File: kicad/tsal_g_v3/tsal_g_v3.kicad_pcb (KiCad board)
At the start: 2 copper layers, 55 x 50 mm, 54 parts, among them J1 Conn_01x02_Pin, J2 Conn_01x02_Pin, J3 Conn_01x03, J4 Conn_01x06, Q1 2N7002, Q2 2N7002, Q4 AO3401A, U1 LTV-817S, U10 TL431DBZ, U3 B1212, U4 BU4SU69G2, U5 BUS4S71G2, U6 BU4S81G2, U7 BU4S81G2, U8 BU4S01G2, U9 BU4S01G2

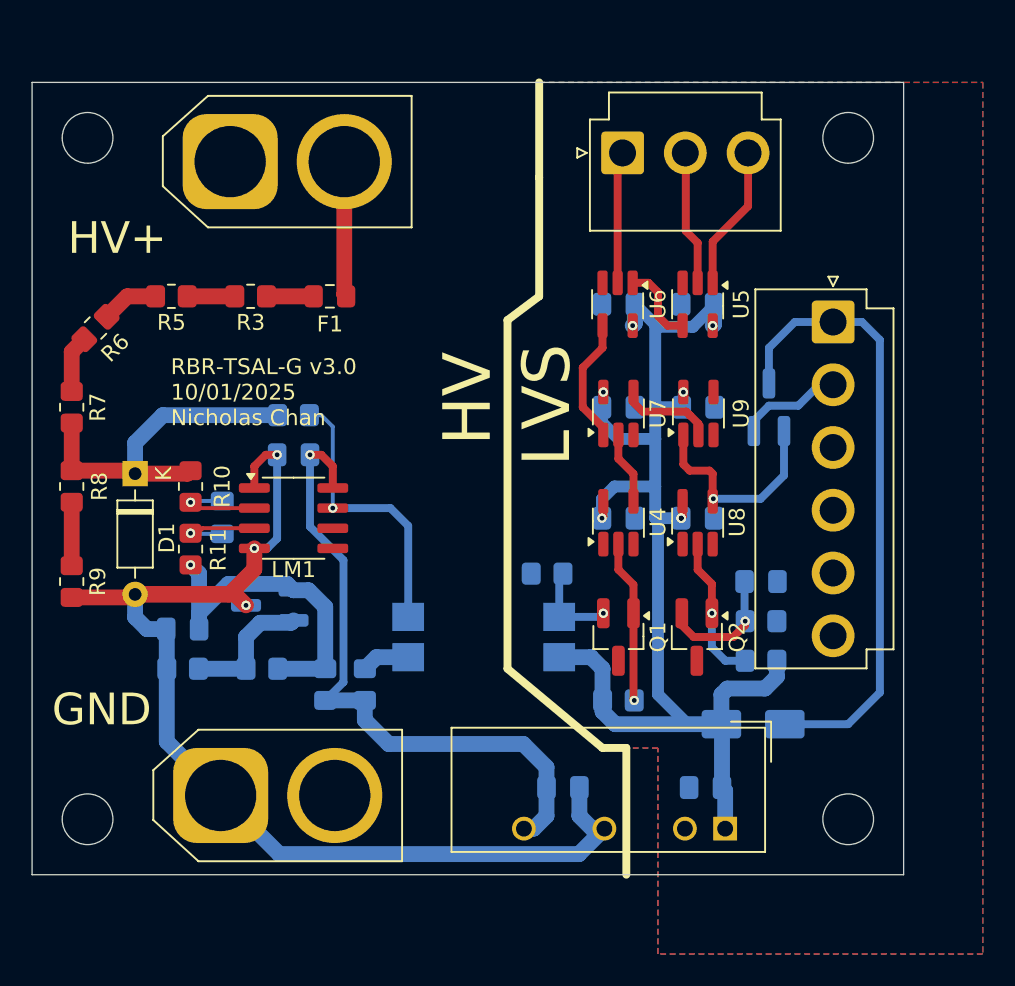
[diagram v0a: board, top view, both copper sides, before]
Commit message: hole seperation to multiples of 3mm
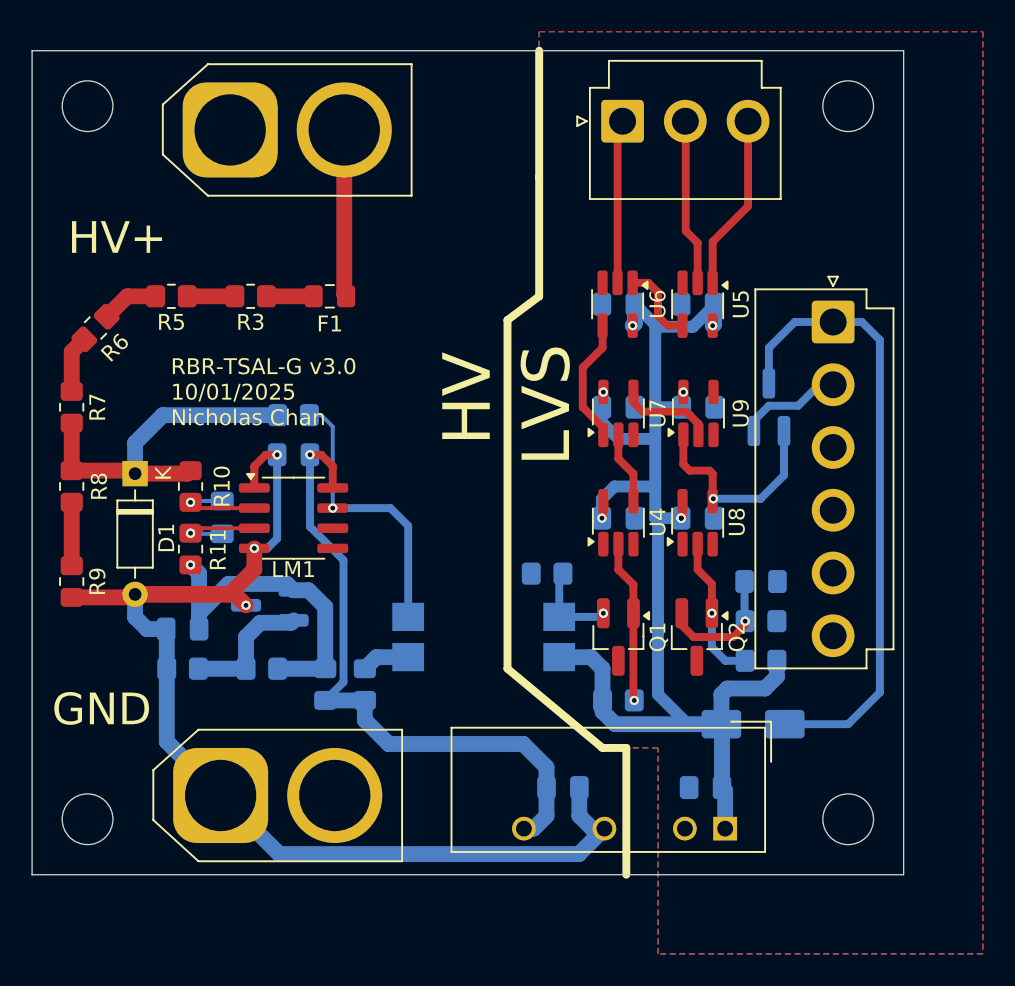
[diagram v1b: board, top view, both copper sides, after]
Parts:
- moved H1 2.00 mm to (153.5, 51.5)
- moved H2 2.00 mm to (201.5, 51.5)
- moved J1 2.00 mm to (162.5, 53.0)
- moved J3 2.00 mm to (187.3, 52.5)
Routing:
- net Out Precharge: track 8.52 -> 10.5 mm
- net Out -: track 8.33 -> 10.3 mm
- net Out +: track 9.12 -> 11.1 mm
- net Net-(J1-Pin_2): track 8.55 -> 10.5 mm
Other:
- board size 55 x 50 mm -> 55 x 52 mm
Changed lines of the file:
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@@
 	(footprint "Connector_JST:JST_VH_B3P-VH_1x03_P3.96mm_Vertical"
 		(layer "F.Cu")
-		(at 187.2625 54.45)
+		(at 187.2625 52.45)
 		(descr "JST VH series connector, B3P-VH (http://www.jst-mfg.com/product/pdf/eng/eVH.pdf), generated with kicad-footprint-generator")
 		(tags "connector JST VH vertical")
@@
 	(footprint "MountingHole:MountingHole_3.2mm_M3"
 		(layer "F.Cu")
-		(at 201.5 53.5)
+		(at 201.5 51.5)
 		(descr "Mounting Hole 3.2mm, no annular, M3")
 		(tags "mounting hole 3.2mm no annular m3")
@@
 	(footprint "Connector_AMASS:AMASS_XT60-M_1x02_P7.20mm_Vertical"
 		(layer "F.Cu")
-		(at 162.5 55)
+		(at 162.5 53)
 		(descr "AMASS female XT60, through hole, vertical, https://www.tme.eu/Document/2d152ced3b7a446066e6c419d84bb460/XT60%20SPEC.pdf")
 		(tags "XT60 female vertical")
@@
 		(tags "SOT-23-5 hand-soldering")
 		(property "Reference" "U8"
-			(at 0.036666 2.5 270)
+			(at 0.036666 2.5 -90)
 			(layer "F.SilkS")
 			(effects
@@
 		)
 		(property "Value" "BU4S01G2"
-			(at 0 2.9 270)
+			(at 0 2.9 -90)
 			(layer "F.Fab")
 			(effects
@@
 		)
 		(fp_text user "${REFERENCE}"
-			(at 0 0 360)
+			(at 0 0 0)
 			(layer "F.Fab")
 			(effects
@@
 		(tags "resistor handsolder")
 		(property "Reference" "R10"
-			(at 0 2 270)
+			(at 0 2 -90)
 			(layer "F.SilkS")
 			(effects
@@
 		)
 		(property "Value" "100"
-			(at 0 1.65 270)
+			(at 0 1.65 -90)
 			(layer "F.Fab")
 			(effects
@@
 		)
 		(fp_text user "${REFERENCE}"
-			(at 0 0 270)
+			(at 0 0 -90)
 			(layer "F.Fab")
 			(effects
@@
 		(tags "SOT-23-5 hand-soldering")
 		(property "Reference" "U7"
-			(at 0 2.5 270)
+			(at 0 2.5 -90)
 			(layer "F.SilkS")
 			(effects
@@
 		)
 		(property "Value" "BU4S81G2 "
-			(at 0 2.9 270)
+			(at 0 2.9 -90)
 			(layer "F.Fab")
 			(effects
@@
 		)
 		(fp_text user "${REFERENCE}"
-			(at 0 0 360)
+			(at 0 0 0)
 			(layer "F.Fab")
 			(effects
@@
 		(tags "resistor handsolder")
 		(property "Reference" "R8"
-			(at 0 1.75 270)
+			(at 0 1.75 -90)
 			(layer "F.SilkS")
 			(effects
@@
 		)
 		(property "Value" "25k"
-			(at 0 1.65 270)
+			(at 0 1.65 -90)
 			(layer "F.Fab")
 			(effects
@@
 		)
 		(fp_text user "${REFERENCE}"
-			(at 0 0 270)
+			(at 0 0 -90)
 			(layer "F.Fab")
 			(effects
@@
 		(tags "SOT-23-5 hand-soldering")
 		(property "Reference" "U4"
-			(at 0.036666 2.5 270)
+			(at 0.036666 2.5 -90)
 			(layer "F.SilkS")
 			(effects
@@
 		)
 		(property "Value" "BU4SU69G2"
-			(at 0 2.9 270)
+			(at 0 2.9 -90)
 			(layer "F.Fab")
 			(effects
@@
 		)
 		(fp_text user "${REFERENCE}"
-			(at 0 0 360)
+			(at 0 0 0)
 			(layer "F.Fab")
 			(effects
@@
 	(footprint "MountingHole:MountingHole_3.2mm_M3"
 		(layer "F.Cu")
-		(at 153.5 53.5)
+		(at 153.5 51.5)
 		(descr "Mounting Hole 3.2mm, no annular, M3")
 		(tags "mounting hole 3.2mm no annular m3")
@@
 		(tags "SOT-23-5 hand-soldering")
 		(property "Reference" "U9"
-			(at 0 2.7 270)
+			(at 0 2.7 -90)
 			(layer "F.SilkS")
 			(effects
@@
 		)
 		(property "Value" "BU4S01G2"
-			(at 0 2.9 270)
+			(at 0 2.9 -90)
 			(layer "F.Fab")
 			(effects
@@
 		)
 		(fp_text user "${REFERENCE}"
-			(at 0 0 360)
+			(at 0 0 0)
 			(layer "F.Fab")
 			(effects
@@
 		)
 		(property "Value" "AO3401A"
-			(at 0 -2.5 270)
+			(at 0 -2.5 -90)
 			(layer "B.Fab")
 			(effects
@@
 		)
 		(fp_text user "${REFERENCE}"
-			(at 0 0 360)
+			(at 0 0 0)
 			(layer "B.Fab")
 			(effects
@@
 		(tags "capacitor handsolder")
 		(property "Reference" "C7"
-			(at -1 1.75 360)
+			(at -1 1.75 0)
 			(layer "B.SilkS")
 			(effects
@@
 		)
 		(property "Value" "0.1uF"
-			(at 0 -1.68 360)
+			(at 0 -1.68 0)
 			(layer "B.Fab")
 			(effects
@@
 		)
 		(fp_text user "${REFERENCE}"
-			(at 0 0 360)
+			(at 0 0 0)
 			(layer "B.Fab")
 			(effects
@@
 		(tags "capacitor handsolder")
 		(property "Reference" "C9"
-			(at -0.75 1.75 360)
+			(at -0.75 1.75 0)
 			(layer "B.SilkS")
 			(effects
@@
 		)
 		(property "Value" "0.1uF"
-			(at 0 -1.68 360)
+			(at 0 -1.68 0)
 			(layer "B.Fab")
 			(effects
@@
 		)
 		(fp_text user "${REFERENCE}"
-			(at 0 0 360)
+			(at 0 0 0)
 			(layer "B.Fab")
 			(effects
@@
 		(tags "Diode SMA (DO-214AC)")
 		(property "Reference" "D2"
-			(at 4.75 0 360)
+			(at 4.75 0 0)
 			(layer "B.SilkS")
 			(effects
@@
 		)
 		(property "Value" "D"
-			(at 0 -2.6 360)
+			(at 0 -2.6 0)
 			(layer "B.Fab")
 			(effects
@@
 		)
 		(fp_text user "${REFERENCE}"
-			(at 0 2.5 360)
+			(at 0 2.5 0)
 			(layer "B.Fab")
 			(effects
@@
 		(tags "capacitor handsolder")
 		(property "Reference" "C5"
-			(at 3 0 360)
+			(at 3 0 0)
 			(layer "B.SilkS")
 			(effects
@@
 		)
 		(property "Value" "2.2uF"
-			(at 0 -1.68 360)
+			(at 0 -1.68 0)
 			(layer "B.Fab")
 			(effects
@@
 		)
 		(fp_text user "${REFERENCE}"
-			(at 0 0 360)
+			(at 0 0 0)
 			(layer "B.Fab")
 			(effects
@@
 		(tags "resistor handsolder")
 		(property "Reference" "R15"
-			(at 0 1.65 360)
+			(at 0 1.65 0)
 			(layer "B.SilkS")
 			(effects
@@
 		)
 		(property "Value" "~"
-			(at 0 -1.65 360)
+			(at 0 -1.65 0)
 			(layer "B.Fab")
 			(effects
@@
 		)
 		(fp_text user "${REFERENCE}"
-			(at 0 0 360)
+			(at 0 0 0)
 			(layer "B.Fab")
 			(effects
@@
 		(tags "resistor handsolder")
 		(property "Reference" "R12"
-			(at 3.75 0 360)
+			(at 3.75 0 0)
 			(layer "B.SilkS")
 			(effects
@@
 		)
 		(property "Value" "1M"
-			(at 0 -1.65 360)
+			(at 0 -1.65 0)
 			(layer "B.Fab")
 			(effects
@@
 		)
 		(fp_text user "${REFERENCE}"
-			(at 0 0 360)
+			(at 0 0 0)
 			(layer "B.Fab")
 			(effects
@@
 		)
 		(property "Value" "2k2"
-			(at 0 -1.65 270)
+			(at 0 -1.65 -90)
 			(layer "B.Fab")
 			(effects
@@
 		)
 		(fp_text user "${REFERENCE}"
-			(at 0 0 270)
+			(at 0 0 -90)
 			(layer "B.Fab")
 			(effects
@@
 		(tags "SMD DIP DIL PDIP SMDIP 2.54mm 9.53mm 375mil")
 		(property "Reference" "U1"
-			(at 0 3.6 360)
+			(at 0 3.6 0)
 			(layer "B.SilkS")
 			(effects
@@
 		)
 		(property "Value" "LTV-817S"
-			(at 0 -3.6 360)
+			(at 0 -3.6 0)
 			(layer "B.Fab")
 			(effects
@@
 		)
 		(fp_text user "${REFERENCE}"
-			(at 0 0 360)
+			(at 0 0 0)
 			(layer "B.Fab")
 			(effects
@@
 		(tags "capacitor handsolder")
 		(property "Reference" "C10"
-			(at -4 0 360)
+			(at -4 0 0)
 			(layer "B.SilkS")
 			(effects
@@
 		)
 		(property "Value" "4.7uF"
-			(at 0 -1.68 360)
+			(at 0 -1.68 0)
 			(layer "B.Fab")
 			(effects
@@
 		)
 		(fp_text user "${REFERENCE}"
-			(at 0 0 360)
+			(at 0 0 0)
 			(layer "B.Fab")
 			(effects
@@
 	)
 	(gr_line
-		(start 182 50)
+		(start 182 48)
 		(end 182 56)
 		(stroke
@@
 	)
 	(gr_rect
-		(start 150 50)
+		(start 150 48)
 		(end 205 100)
 		(stroke
@@
 	)
 	(segment
-		(start 195.1825 54.45)
-		(end 195.1825 57.8175)
+		(start 192.95 60.05)
+		(end 192.95 62.65)
 		(width 0.5)
 		(layer "F.Cu")
@@
 	)
 	(segment
-		(start 192.95 60.05)
-		(end 192.95 62.65)
+		(start 195.1825 52.45)
+		(end 195.1825 57.8175)
 		(width 0.5)
 		(layer "F.Cu")
@@
 	)
 	(segment
-		(start 191.25 54.4775)
-		(end 191.25 59.375)
+		(start 192 60.125)
+		(end 192 62.65)
 		(width 0.5)
 		(layer "F.Cu")
@@
 	)
 	(segment
-		(start 191.2225 54.45)
-		(end 191.25 54.4775)
+		(start 191.25 59.375)
+		(end 192 60.125)
 		(width 0.5)
 		(layer "F.Cu")
@@
 	)
 	(segment
-		(start 191.25 59.375)
-		(end 192 60.125)
+		(start 191.2225 52.45)
+		(end 191.25 52.4775)
 		(width 0.5)
 		(layer "F.Cu")
@@
 	)
 	(segment
-		(start 192 60.125)
-		(end 192 62.65)
+		(start 191.25 52.4775)
+		(end 191.25 59.375)
 		(width 0.5)
 		(layer "F.Cu")
@@
 	)
 	(segment
-		(start 187.2625 54.45)
-		(end 186.95 54.7625)
+		(start 186.95 52.7625)
+		(end 186.95 62.65)
 		(width 0.5)
 		(layer "F.Cu")
@@
 	)
 	(segment
-		(start 186.95 54.7625)
-		(end 186.95 62.65)
+		(start 187.2625 52.45)
+		(end 186.95 52.7625)
 		(width 0.5)
 		(layer "F.Cu")
@@
 	)
 	(segment
-		(start 169.7 55)
-		(end 169.7 63.382107)
+		(start 169.7 63.382107)
+		(end 169.817893 63.5)
 		(width 1)
 		(layer "F.Cu")
@@
 	)
 	(segment
-		(start 169.7 63.382107)
-		(end 169.817893 63.5)
+		(start 169.7 53)
+		(end 169.7 63.382107)
 		(width 1)
 		(layer "F.Cu")
@@
 		(polygon
 			(pts
-				(xy 182 50) (xy 210 50) (xy 210 105) (xy 189.5 105) (xy 189.5 92) (xy 186 92) (xy 180 87) (xy 180 65)
+				(xy 182 46.8) (xy 210 46.8) (xy 210 105) (xy 189.5 105) (xy 189.5 92) (xy 186 92) (xy 180 87) (xy 180 65)
 				(xy 182 63.5)
 			)
